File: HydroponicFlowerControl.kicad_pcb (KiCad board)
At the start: 4 copper layers, 101 x 101 mm, 228 parts, among them IC1 ADM3260ARSZ-RL7, IC2 ADM3260ARSZ-RL7, IC3 CH224K, J1 EC, J10 Pump 1, J11 Temperature, J12 Pump 2, J13 Pump 3, J14 D IN1, J15 D IN2, J16 D IN3, J17 CAN, J18 Raspberry_Pi_2_3, J19 Conn_ARM_JTAG_SWD_10, J2 Temp, J20 Conn_ARM_JTAG_SWD_10, J21 Conn_01x04_Pin, J22 1-Wire, J25 Conn_01x03_Socket, J26 Conn_01x03_Socket, J3 Flow, J4 pH, J5 USB_C_Receptacle_USB2.0, J6 Barrel_Jack, J7 Valve 1, J8 Valve 2, J9 Valve 3, Q1 MMBT3904, Q10 AO3401A, Q11 MMBT3904, Q12 AO3401A, Q2 AO3401A, Q3 MMBT3904, Q4 AO3401A, Q5 MMBT3904, Q6 AO3401A, Q7 MMBT3904, Q8 MMBT3904, Q9 AO3401A, SW1 RESET, SW2 BOOT, U1 AT24C256C, U13 TPD2EUSB30, U16 MCP2518FD-xQBB, U17 HDC1080, U18 SN65HVD230, U19 SN65HVD230, U2 ADS1115IDGS, U20 TPS5430DDA, U4 TPS60400DBV, U5 LM324, U6 MCP4017T-502E/LT, U7 LM358, U8 STM32G473CBTx, U9 AMS1117-3.3, Y1 8 MHz, Y2 40MHz

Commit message: Move buttons
Closes #45
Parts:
- moved R77 42.0 mm to (130.1, 155.2)
- moved SW2 42.0 mm to (135.2, 156.8)
- moved C51 41.9 mm to (134.3, 145.0)
- moved R65 41.9 mm to (134.3, 146.7)
- moved SW1 41.9 mm to (134.8, 150.6)
- moved TP12 0.51 mm to (134.5, 117.3)
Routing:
- net +3.3V: track 83.8 -> 143.7 mm, vias 23 -> 22
- net BOOT0: track 41.5 -> 88.9 mm
- net ~{RESET}: track 87.3 -> 132.8 mm, vias 2 -> 4
- net GND: track 170.2 -> 166.9 mm
- net +5V: track 41.4 -> 39.9 mm
- net /RaspberryPi/SPI_SCK: track 42.5 -> 41.1 mm

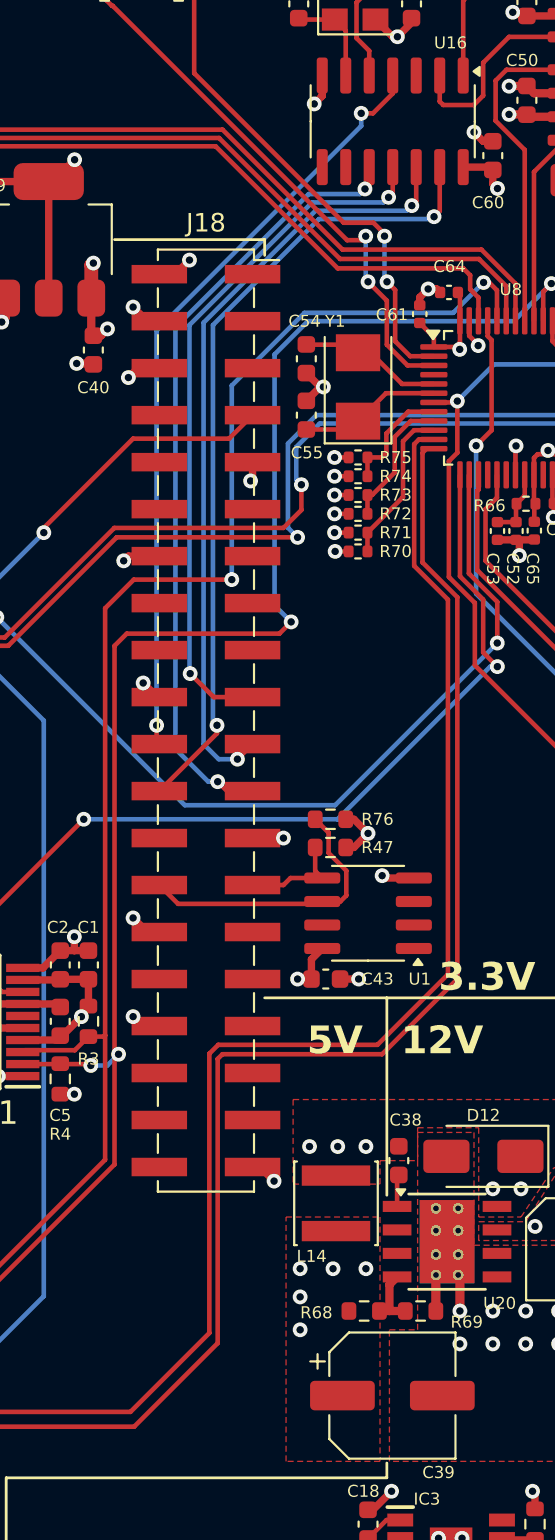
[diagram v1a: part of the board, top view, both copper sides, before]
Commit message: Replace footprint for J18
Closes #31
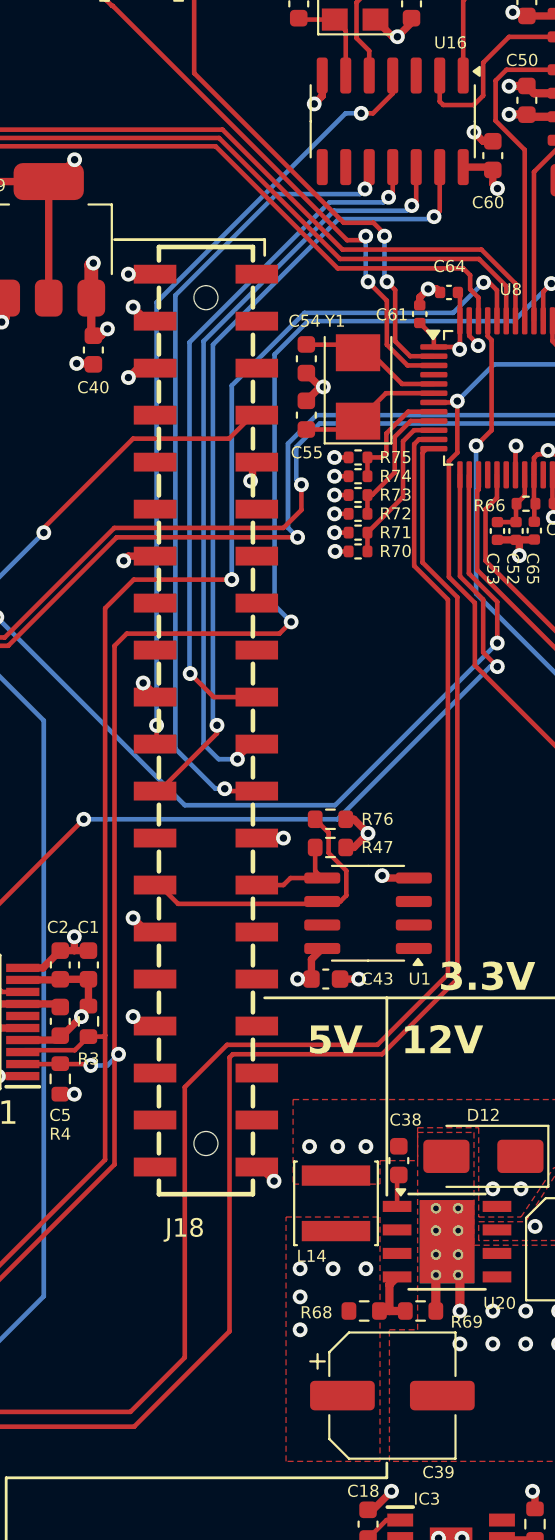
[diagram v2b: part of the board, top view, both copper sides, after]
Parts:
- J18: footprint Connector_PinSocket_2.54mm:PinSocket_2x20_P2.54mm_Vertical_SMD -> HydroponicFlowerControl:HDR-SMD_40P-P2.54-V-F-R2-C20-S7.1-EH
- turned J18 to -90 degrees
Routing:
- net /RaspberryPi/SPI_SCK: track 41.1 -> 43.8 mm
- net /RaspberryPi/~{SPI_CS}: track 43.8 -> 43.1 mm
- net /RaspberryPi/SPI_MISO: track 42.2 -> 41.6 mm
- net /RaspberryPi/SPI_MOSI: track 38.1 -> 37.6 mm

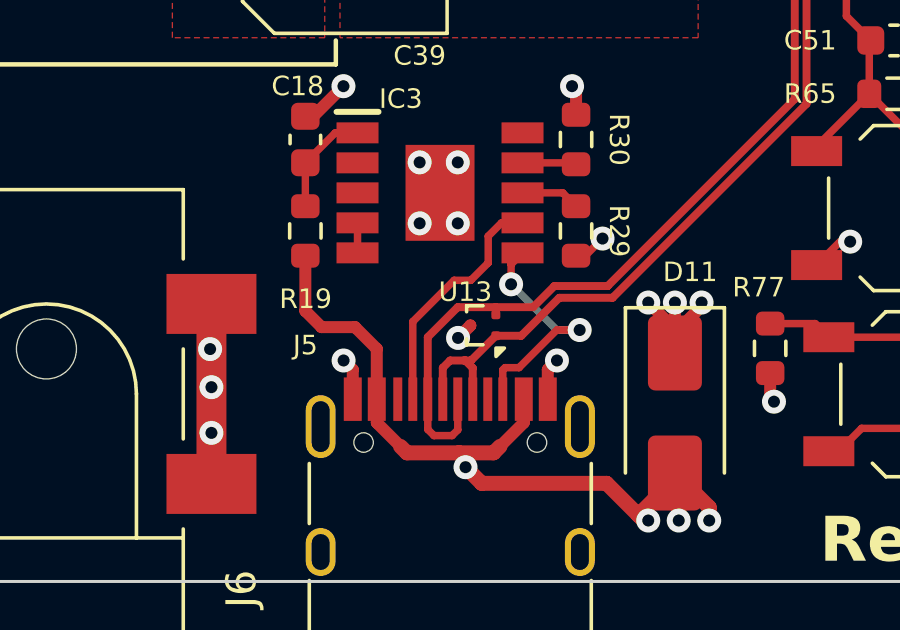
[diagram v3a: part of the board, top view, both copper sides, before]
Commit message: Update footprint for U13
Closes #33
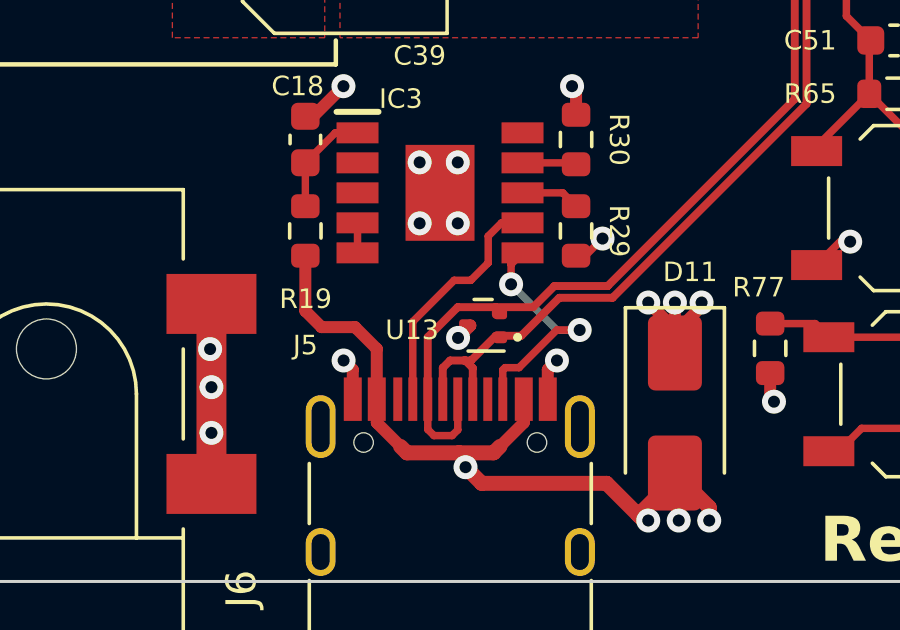
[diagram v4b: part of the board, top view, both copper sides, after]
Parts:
- U13: footprint Package_TO_SOT_SMD:Texas_DRT-3 -> Package_TO_SOT_SMD:SOT-723
- turned U13 to 180 degrees
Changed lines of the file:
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@@
 		)
 	)
-	(footprint "Package_TO_SOT_SMD:Texas_DRT-3"
+	(footprint "Package_TO_SOT_SMD:SOT-723"
 		(layer "F.Cu")
-		(at 120.567 154.46 90)
-		(descr "Texas Instrument DRT-3 1x0.8mm Pitch 0.7mm http://www.ti.com/lit/ds/symlink/tpd2eusb30.pdf")
-		(tags "DRT-3 1x0.8mm Pitch 0.7mm")
+		(at 120.567 154.46 180)
+		(descr "http://toshiba.semicon-storage.com/info/docget.jsp?did=5879&prodName=RN1104MFV")
+		(tags "sot 723")
 		(property "Reference" "U13"
-			(at 1.112 -0.591 180)
+			(at 2.369 -0.158 0)
 			(layer "F.SilkS")
 			(effects
@@
 		)
 		(property "Value" "TPD2EUSB30"
-			(at 0 1.5 90)
+			(at 0 1.75 0)
 			(layer "F.Fab")
 			(effects
@@
 			)
 		)
-		(property "Footprint" "Package_TO_SOT_SMD:Texas_DRT-3"
-			(at 0 0 90)
+		(property "Footprint" "Package_TO_SOT_SMD:SOT-723"
+			(at 0 0 180)
 			(unlocked yes)
 			(layer "F.Fab")
@@
 			)
 		)
-		(property "Datasheet" "http://www.ti.com/lit/ds/symlink/tpd2eusb30a.pdf"
-			(at 0 0 90)
+		(property "Datasheet" "https://www.lcsc.com/datasheet/lcsc_datasheet_2411121100_TECH-PUBLIC-TPD2EUSB30DRTR-TP_C2844720.pdf"
+			(at 0 0 180)
 			(unlocked yes)
 			(layer "F.Fab")
@@
 		)
 		(property "Description" "2-Channel ESD Protection for Super-Speed USB 3.0 Interface, DRT-3"
-			(at 0 0 90)
+			(at 0 0 180)
 			(unlocked yes)
 			(layer "F.Fab")
@@
 		)
 		(property "LCSC" "C2844720"
-			(at 0 0 90)
+			(at 0 0 180)
 			(unlocked yes)
 			(layer "F.Fab")
@@
 			(effects
 				(font
-					(size 1 1)
-					(thickness 0.15)
+					(size 0.65 0.65)
+					(thickness 0.1)
 				)
 			)
@@
 		(attr smd)
 		(fp_line
-			(start 0.65 -0.55)
-			(end 0.45 -0.55)
+			(start 0.5 -0.86)
+			(end -0.7 -0.86)
 			(stroke
 				(width 0.12)
@@
 		)
 		(fp_line
-			(start -0.65 -0.55)
-			(end -0.45 -0.55)
+			(start 0.3 0.86)
+			(end -0.3 0.86)
 			(stroke
 				(width 0.12)
@@
 			(layer "F.SilkS")
 		)
-		(fp_line
-			(start 0.65 0)
-			(end 0.65 -0.55)
+		(fp_circle
+			(center -1.15 -0.4)
+			(end -1 -0.4)
 			(stroke
-				(width 0.12)
+				(width 0)
 				(type solid)
 			)
+			(fill solid)
 			(layer "F.SilkS")
 		)
 		(fp_line
-			(start -0.65 0)
-			(end -0.65 -0.55)
-			(stroke
-				(width 0.12)
-				(type solid)
-			)
-			(layer "F.SilkS")
-		)
-		(fp_poly
-			(pts
-				(xy -0.76 0.43) (xy -0.76 0.71) (xy -1.04 0.43) (xy -0.76 0.43)
-			)
+			(start 0.9 0.9)
+			(end -0.9 0.9)
 			(stroke
-				(width 0.12)
+				(width 0.05)
 				(type solid)
 			)
-			(fill solid)
-			(layer "F.SilkS")
+			(layer "F.CrtYd")
 		)
 		(fp_line
-			(start 0.8 -0.7)
-			(end 0.8 0.7)
+			(start 0.9 -0.9)
+			(end 0.9 0.9)
 			(stroke
 				(width 0.05)
@@
 		)
 		(fp_line
-			(start -0.8 -0.7)
-			(end 0.8 -0.7)
+			(start -0.9 0.9)
+			(end -0.9 -0.9)
 			(stroke
 				(width 0.05)
@@
 		)
 		(fp_line
-			(start 0.8 0.7)
-			(end -0.8 0.7)
+			(start -0.9 -0.9)
+			(end 0.9 -0.9)
 			(stroke
 				(width 0.05)
@@
 		)
 		(fp_line
-			(start -0.8 0.7)
-			(end -0.8 -0.7)
+			(start -0.9 -0.9)
+			(end -0.9 -0.9)
 			(stroke
 				(width 0.05)
@@
 		)
 		(fp_line
-			(start 0.5 -0.4)
-			(end 0.5 0.4)
+			(start 0.4 0.6)
+			(end -0.4 0.6)
 			(stroke
 				(width 0.1)
@@
 		)
 		(fp_line
-			(start -0.5 -0.4)
-			(end 0.5 -0.4)
+			(start 0.4 -0.6)
+			(end 0.4 0.6)
 			(stroke
 				(width 0.1)
@@
 		)
 		(fp_line
-			(start -0.5 0.1)
-			(end -0.5 -0.4)
+			(start -0.1 -0.6)
+			(end 0.4 -0.6)
 			(stroke
 				(width 0.1)
@@
 		)
 		(fp_line
-			(start -0.5 0.1)
-			(end -0.2 0.4)
+			(start -0.4 0.6)
+			(end -0.4 -0.3)
 			(stroke
 				(width 0.1)
@@
 		)
 		(fp_line
-			(start 0.5 0.4)
-			(end -0.2 0.4)
+			(start -0.4 -0.3)
+			(end -0.1 -0.6)
 			(stroke
 				(width 0.1)
@@
 		)
 		(fp_text user "${REFERENCE}"
-			(at 0 -1.5 90)
+			(at 0.8 0 90)
 			(layer "F.Fab")
 			(effects
 				(font
-					(size 1 1)
-					(thickness 0.15)
+					(size 0.5 0.5)
+					(thickness 0.075)
 				)
 			)
 		)
 		(pad "1" smd roundrect
-			(at -0.35 0.425 90)
-			(size 0.3 0.3)
+			(at -0.575 -0.4 180)
+			(size 0.45 0.4)
 			(layers "F.Cu" "F.Paste" "F.Mask")
 			(roundrect_rratio 0.25)
@@
 		)
 		(pad "2" smd roundrect
-			(at 0.35 0.425 90)
-			(size 0.3 0.3)
+			(at -0.575 0.4 180)
+			(size 0.45 0.4)
 			(layers "F.Cu" "F.Paste" "F.Mask")
 			(roundrect_rratio 0.25)
@@
 		)
 		(pad "3" smd roundrect
-			(at 0 -0.425 90)
-			(size 0.3 0.3)
+			(at 0.575 0 180)
+			(size 0.45 0.4)
 			(layers "F.Cu" "F.Paste" "F.Mask")
 			(roundrect_rratio 0.25)
@@
 			(pintype "passive")
 		)
-		(model "${KICAD8_3DMODEL_DIR}/Package_TO_SOT_SMD.3dshapes/Texas_DRT-3.wrl"
+		(model "${KICAD8_3DMODEL_DIR}/Package_TO_SOT_SMD.3dshapes/SOT-723.wrl"
 			(offset
 				(xyz 0 0 0)
@@
 	)
 	(segment
-		(start 120.992 154.11)
+		(start 122.238814 153.856)
 		(end 120.992 153.856)
 		(width 0.265)
-		(locked yes)
 		(layer "F.Cu")
 		(net 192)
@@
 	)
 	(segment
-		(start 120.992 153.856)
-		(end 119.722 153.856)
-		(width 0.265)
-		(locked yes)
-		(layer "F.Cu")
-		(net 192)
-	)
-	(segment
 		(start 124.720814 153.152)
 		(end 122.942814 153.152)
@@
 	)
 	(segment
+		(start 120.992 153.856)
+		(end 119.722 153.856)
+		(width 0.265)
+		(layer "F.Cu")
+		(net 192)
+	)
+	(segment
 		(start 130.956 146.916814)
 		(end 124.720814 153.152)
@@
 	)
 	(segment
-		(start 122.238814 153.856)
+		(start 120.992 154.11)
 		(end 120.992 153.856)
 		(width 0.265)
-		(locked yes)
 		(layer "F.Cu")
 		(net 192)

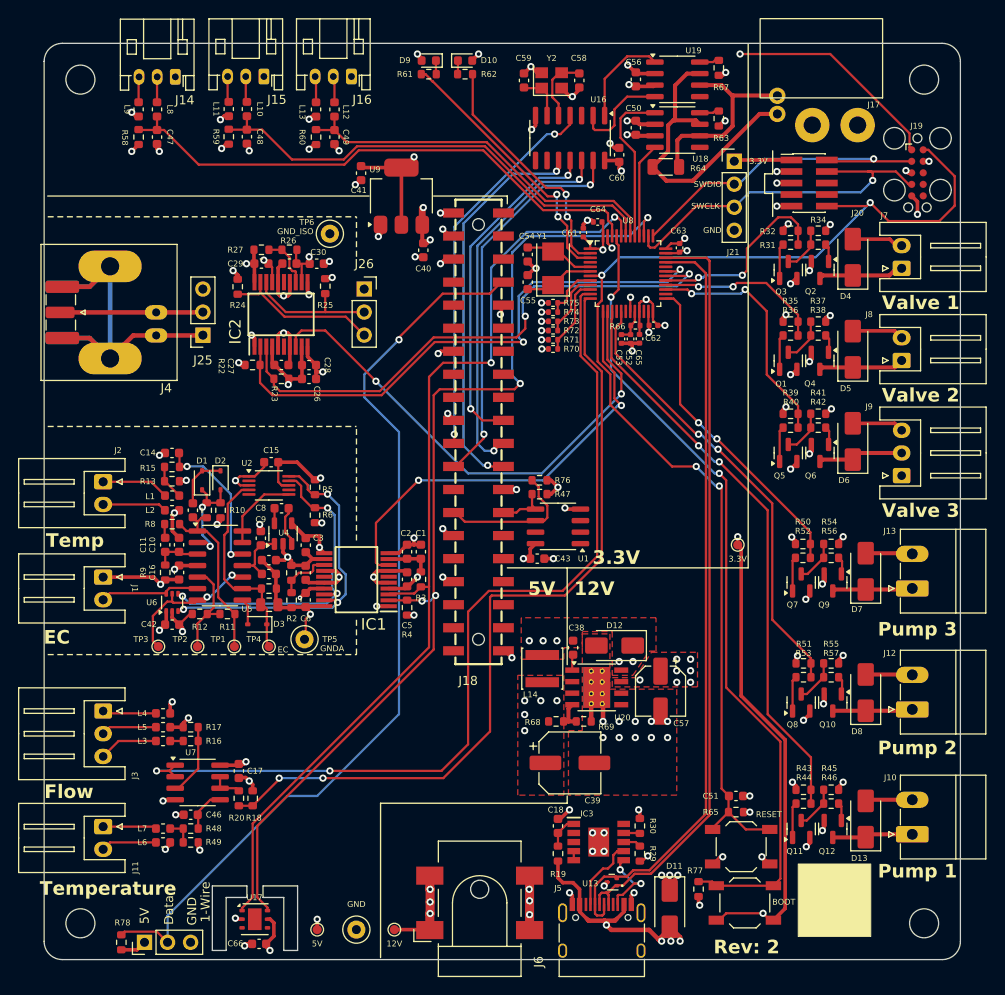
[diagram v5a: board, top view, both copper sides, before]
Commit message: Add testpoints
Closes #47
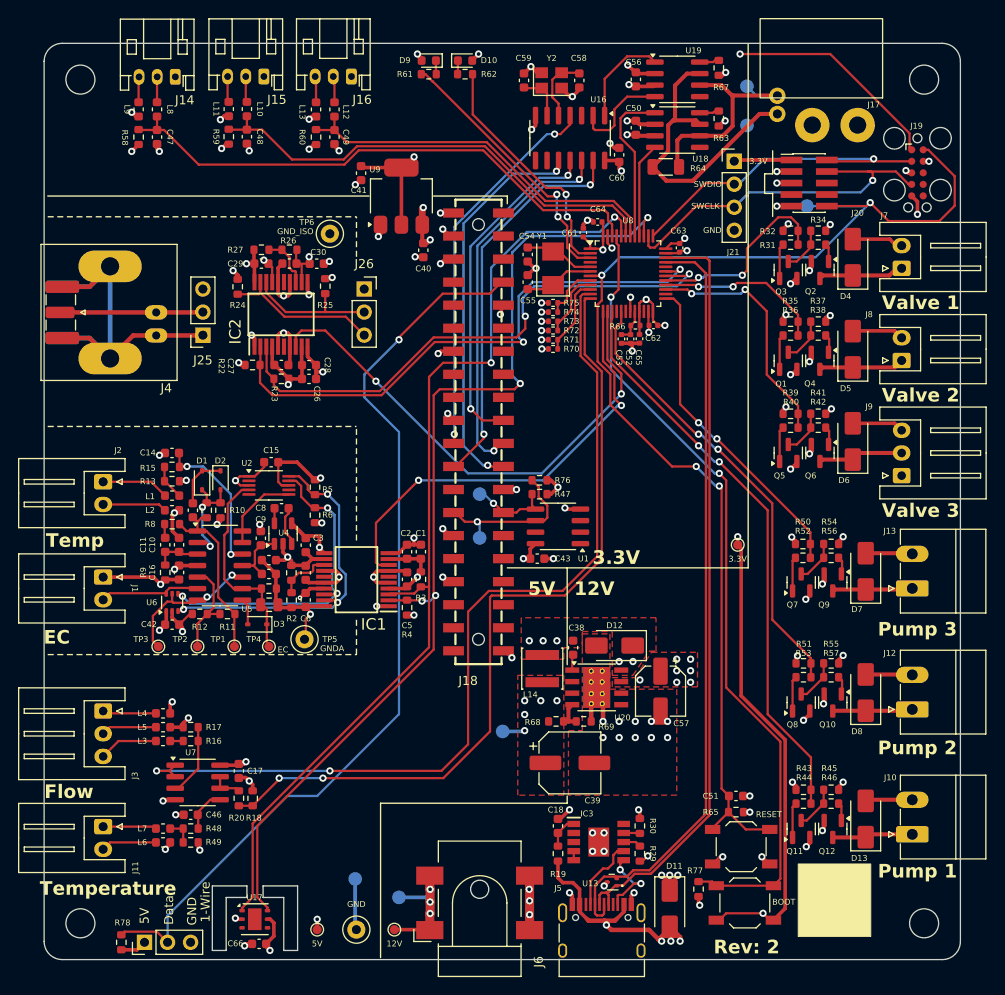
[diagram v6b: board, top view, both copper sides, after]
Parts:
- added TP14: ID_SCL, TestPoint:TestPoint_Pad_D1.5mm, B.Cu at (106.0, 116.5)
- added TP15: 12V, TestPoint:TestPoint_Pad_D1.5mm, B.Cu at (97.1, 156.1)
- added TP16: 5V, TestPoint:TestPoint_Pad_D1.5mm, B.Cu at (108.5, 137.9)
- added TP17: GND, TestPoint:TestPoint_Pad_D1.5mm, B.Cu at (92.3, 154.1)
- added TP18: Reset, TestPoint:TestPoint_Pad_D1.5mm, B.Cu at (142.1, 79.9)
- added TP7: CANH, TestPoint:TestPoint_Pad_D1.5mm, B.Cu at (135.5, 71.1)
- added TP8: CANL, TestPoint:TestPoint_Pad_D1.5mm, B.Cu at (135.5, 66.7)
- added TP9: ID_SDA, TestPoint:TestPoint_Pad_D1.5mm, B.Cu at (106.0, 111.7)
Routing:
- net ~{RESET}: track 132.8 -> 140.0 mm
- net GND: track 166.9 -> 172.5 mm
- net /MCU/CAN_H: track 33.7 -> 37.6 mm
- net /MCU/CAN_L: track 21.4 -> 25.1 mm
- net +12V: track 26.6 -> 30.3 mm
- net /RaspberryPi/ID_SDA: track 5.74 -> 9.20 mm, vias 0 -> 1
- net +5V: track 40.4 -> 42.8 mm
- net /RaspberryPi/ID_SCL: track 15.4 -> 17.2 mm, vias 0 -> 1
